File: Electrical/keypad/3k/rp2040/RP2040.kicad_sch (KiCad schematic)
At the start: 73 parts, among them J1 Conn_01x04_Socket, P1 USB-TYPE-C-016, Q1 BSS138, SW1 TS-1187A-B-A-B, SW2 TS-1187A-B-A-B, SW3 BUTT1, SW4 BUTT2, SW5 BUTT3, U1 PRTR5V0U2X, U2 ME6208A44M3G, U3 RP2040, U4 ME6212C25M5G, U5 W25Q16JVSS, U6 ME6212C33M5G, U7 SLSS49E, U8 SLSS49E, U9 SLSS49E, Y1 12MHz

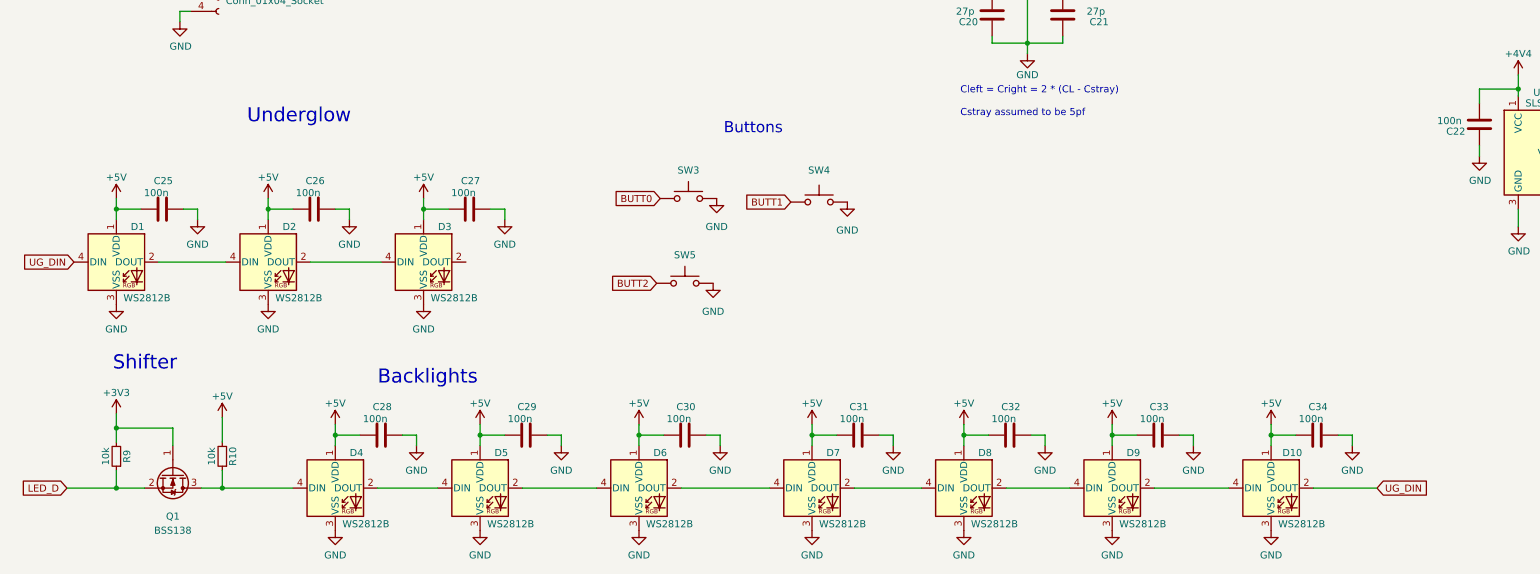
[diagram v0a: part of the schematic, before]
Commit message: uses backlight to refer to individual key lights, and underglow for the rest
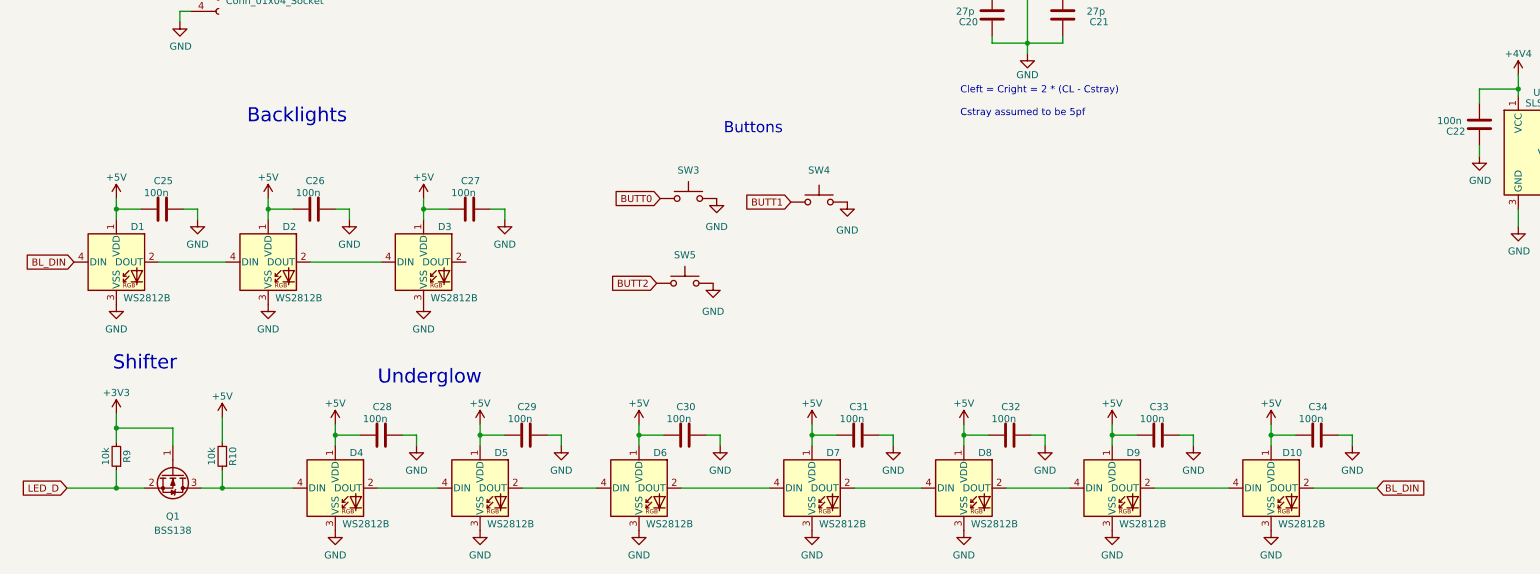
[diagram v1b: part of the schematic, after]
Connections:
- net UG_DIN renamed BL_DIN
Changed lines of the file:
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@@
     (effects (font (size 1.27 1.27)) (justify left bottom))
   )
-  (text "Backlights" (at 78.105 247.015 0)
+  (text "Underglow" (at 78.105 247.015 0)
     (effects (font (size 2.54 2.54)) (justify left bottom))
   )
@@
     (effects (font (size 2 2)) (justify left bottom))
   )
-  (text "Underglow" (at 54.61 200.025 0)
+  (text "Backlights" (at 54.61 200.025 0)
     (effects (font (size 2.54 2.54)) (justify left bottom))
   )
@@
     )
   )
-  (global_label "UG_DIN" (shape input) (at 23.495 224.79 180) (fields_autoplaced)
-    (effects (font (size 1.27 1.27)) (justify right))
-    (property "Intersheetrefs" "${INTERSHEET_REFS}" (at 14.47 224.79 0)
+  (global_label "BL_DIN" (shape input) (at 23.495 224.79 180) (fields_autoplaced)
+    (effects (font (size 1.27 1.27)) (justify right))
+    (property "Intersheetrefs" "${INTERSHEET_REFS}" (at 14.7724 224.79 0)
       (effects (font (size 1.27 1.27)) (justify right) hide)
     )
@@
     )
   )
-  (global_label "UG_DIN" (shape input) (at 257.81 265.43 0) (fields_autoplaced)
-    (effects (font (size 1.27 1.27)) (justify left))
-    (property "Intersheetrefs" "${INTERSHEET_REFS}" (at 266.835 265.43 0)
-      (effects (font (size 1.27 1.27)) (justify left) hide)
-    )
+  (global_label "BL_DIN" (shape input) (at 257.81 265.43 0) (fields_autoplaced)
+    (effects (font (size 1.27 1.27)) (justify left))
+    (property "Intersheetrefs" "${INTERSHEET_REFS}" (at 266.5326 265.43 0)
+      (effects (font (size 1.27 1.27)) (justify left) hide)
+    )

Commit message: saves latest progress
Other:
- moved on the sheet: C20, C21, R8, Y1

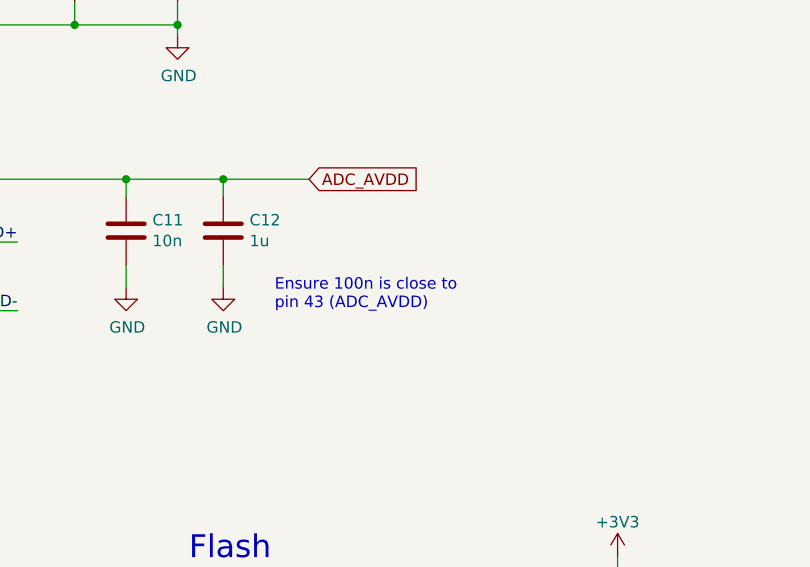
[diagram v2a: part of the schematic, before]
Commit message: finishes rp2040 2 layer board with split gnd
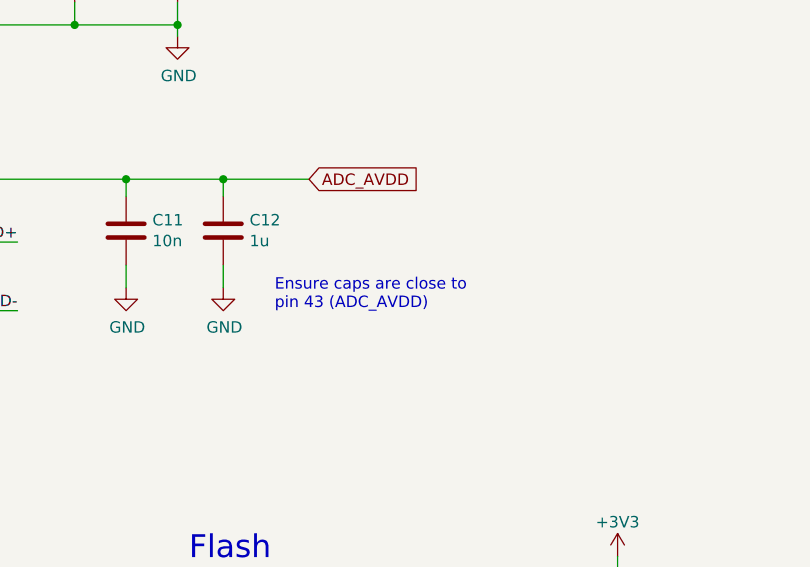
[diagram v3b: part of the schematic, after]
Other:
- note added: "Ensure caps are close to pin 43 (ADC_AVDD)"
- note removed: "Ensure 100n is close to pin 43 (ADC_AVDD)"
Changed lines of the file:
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@@
     (effects (font (size 2.54 2.54)) (justify left bottom))
   )
-  (text "Ensure 100n is close to \npin 43 (ADC_AVDD)" (at 193.04 74.295 0)
+  (text "Ensure caps are close to\npin 43 (ADC_AVDD)" (at 193.04 74.295 0)
     (effects (font (size 1.27 1.27)) (justify left bottom))
   )

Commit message: removes all power supplies except 3v3 and moves some things around in schematic
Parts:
- removed C14, C15, C16, C17: 10u, Capacitor_SMD:C_1206_3216Metric, symbol Device:C
- removed U2: ME6208A44M3G, Package_TO_SOT_SMD:SOT-23-3, symbol Regulator_Linear:ME6208A44M3G
- removed U4: ME6212C25M5G, Package_TO_SOT_SMD:SOT-23-5, symbol Regulator_Linear:AP2127K-3.3
- C18, C19: value 10u -> 1u
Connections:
- net +4V4 is gone; now on net +3V3: C22.2, C23.2, C24.2, U7.1 (VCC), U8.1 (VCC), U9.1 (VCC)
- net ADC_AVDD is gone; now on net +3V3: C11.1, C12.1, U3.43 (ADC_AVDD)
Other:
- note added: "Caps can be ceramic"
- note added: "Per-key Backlights"
- note added: "Power"
- note removed: "ADC VREF"
- note removed: "Backlights"
- note removed: "Do not connect more than 3 sensors because dropout voltage increases with current"
- note removed: "MCU Power"
- note removed: "Sensor Power"
- moved on the sheet: C1, C10, C11, C12, C13, C18, C19, C2, C20, C21, C22, C23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

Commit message: adds all circuit components needed for final pcb, but may need more LED
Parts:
- removed Q1: BSS138, Package_TO_SOT_SMD:SOT-23, symbol Transistor_FET:BSS138
- removed SW3: BUTT1, Button_Switch_SMD:SW_Push_1P1T_NO_6x6mm_H9.5mm, symbol Switch:SW_Push
- removed SW4: BUTT2, Button_Switch_SMD:SW_Push_1P1T_NO_6x6mm_H9.5mm, symbol Switch:SW_Push
- removed SW5: BUTT3, Button_Switch_SMD:SW_Push_1P1T_NO_6x6mm_H9.5mm, symbol Switch:SW_Push
- added C21, C22, C23, C31, C32, C33, C34: 100n, Capacitor_SMD:C_0402_1005Metric, symbol Device:C
- added D10, D11, D8, D9: WS2812B, LED_SMD:LED_WS2812B_PLCC4_5.0x5.0mm_P3.2mm, symbol LED:WS2812B
- added J1: Conn_01x04_Socket, Connector_PinSocket_2.54mm:PinSocket_1x04_P2.54mm_Vertical, symbol Connector:Conn_01x04_Socket
- added R10, R11, R9: 5.1k, Capacitor_SMD:C_0402_1005Metric, symbol Device:R
- added R14, R15: 10k, Resistor_SMD:R_0402_1005Metric, symbol Device:R_Small
- added SW1, SW2, SW3: KAN0644-0551B1-A, push_button_keypad:KAN0644, symbol push_buttons_keypad:KAN0644
- added T1: BSS138BKS_115, Package_TO_SOT_SMD:SOT-363_SC-70-6, symbol BSS138BKS_115:BSS138BKS_115
- renumbered C19 to C10, C13 to C11, C9 to C12, C10 to C13, C11 to C14, C12 to C15, C20 to C16, C21 to C17, C22 to C18, C23 to C19, C24 to C20, C28 to C24, C29 to C25, C30 to C26, C31 to C27, C32 to C28, C33 to C29, C34 to C30, C25 to C35, C26 to C36, C27 to C37, C18 to C9, D4 to D1, D1 to D12, D2 to D13, D3 to D14, D5 to D2, D6 to D3, D7 to D4, D8 to D5, D9 to D6, D10 to D7, J1 to J2, R5 to R1, R9 to R12, R10 to R13, R6 to R2, R1 to R5, R2 to R6, R8 to R7, R7 to R8, SW1 to SW4, SW2 to SW5, U6 to U1, U5 to U2, U1 to U3, U3 to U4, U7 to U5, U8 to U6, U9 to U7
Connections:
- net +3V3: now also R14.2, T1.2, T1.5
- net +5V: now also C31.1, C32.1, C33.1, C34.1, D10.1 (VDD), D11.1 (VDD), D8.1 (VDD), D9.1 (VDD), R15.2
- net ADC_IN1: now also C21.2, R9.2; no longer U5.2 (VOUT)
- net ADC_IN2: now also C22.2, R10.2; no longer U6.2 (VOUT)
- net ADC_IN3: now also C23.2, R11.2; no longer U7.2 (VOUT)
- net BUTT0: now also SW1.1
- net BUTT1: now also SW2.1
- net BUTT2: now also SW3.1
- net GND: now also C21.1, C22.1, C23.1, C31.2, C32.2, C33.2, C34.2, D10.3 (VSS), D11.3 (VSS), D8.3 (VSS), D9.3 (VSS), SW1.2, SW2.2, SW3.2
- net at D1.4 (DIN), R13.1: now also T1.6
- net BL_DIN: no longer names the net of D12.4 (DIN)
- net BL_DIN: now also R15.1, T1.3; no longer D7.2 (DOUT)
- net GPIO10 renamed SDA_1
- net SDA_1: now also J1.1 (Pin_1)
- net GPIO11 renamed SCL_1
- net SCL_1: now also J1.2 (Pin_2)
- net GPIO13 renamed BL_LED_D
- net BL_LED_D: now also R14.1, T1.4
- net GPIO20 renamed SDA_0
- net SDA_0: now also J1.3 (Pin_3)
- net GPIO21 renamed SCL_0
- net SCL_0: now also J1.4 (Pin_4)
- net LED_D renamed U_LED_D
- net U_LED_D: now also T1.1
- new net: D8.2 (DOUT), D9.4 (DIN)
- new net: D7.2 (DOUT), D8.4 (DIN)
- new net: R11.1, U7.2 (VOUT)
- new net: R10.1, U6.2 (VOUT)
- new net: D10.2 (DOUT), D11.4 (DIN)
- new net: D10.4 (DIN), D9.2 (DOUT)
- new net: R9.1, U5.2 (VOUT)
- no-connect marks 2 -> 5
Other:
- moved on the sheet: C11, C16, C17, C18, C19, C20, C24, C25, C26, C27, C28, C29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

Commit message: reverts to using standard bs138 because the dual package one is more expensive than just using two of them, and it's easier to layout
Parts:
- removed T1: BSS138BKS_115, Package_TO_SOT_SMD:SOT-363_SC-70-6, symbol BSS138BKS_115:BSS138BKS_115
- added Q1, Q2: BSS138, Package_TO_SOT_SMD:SOT-23, symbol Transistor_FET:BSS138
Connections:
- net +3V3: now also Q1.1 (G), Q2.1 (G)
- net BL_LED_D: now also U4.15 (GPIO12), Q2.2 (S); no longer U4.16 (GPIO13)
- net U_LED_D: now also U4.16 (GPIO13), Q1.2 (S); no longer U4.15 (GPIO12)
- net at D12.4 (DIN), R15.1: now also Q2.3 (D)
- net at D1.4 (DIN), R13.1: now also Q1.3 (D)
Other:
- moved on the sheet: R10, R11, R9
